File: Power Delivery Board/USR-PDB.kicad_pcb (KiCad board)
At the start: 2 copper layers, 110 x 150 mm, 35 parts, among them U1 XT90, U10 Anderson PP45 Vert. 2x1, U11 Anderson PP45 Vert. 2x1, U12 Anderson PP45 Vert. 2x1, U13 LM2575-5.0BT, U14 MCP3002-I/P, U2 Anderson PP45 Vert. 2x1, U3 Anderson PP45 Vert. 2x1, U4 Anderson PP45 Vert. 2x1, U5 Anderson PP45 Vert. 2x1, U6 Anderson PP45 Vert. 2x1, U7 LM2676T-12_NOPB

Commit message: updated PDB and analog board
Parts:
- added C8: 10uF, Capacitor_SMD:C_0805_2012Metric_Pad1.18x1.45mm_HandSolder, F.Cu at (125.5, 66.0)
- added C9: 10uF, Capacitor_SMD:C_0805_2012Metric_Pad1.18x1.45mm_HandSolder, F.Cu at (125.5, 59.5)
- added U17: AMS1117-3.3, USR:SOT_AMS1117-2.5_AMS, F.Cu at (118.5, 62.8)
- C1, C4: footprint Capacitor_THT:C_Disc_D5.0mm_W2.5mm_P2.50mm -> Capacitor_THT:C_Disc_D16.0mm_W5.0mm_P10.00mm
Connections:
- C6 pad 1: /5V_OUT -> 5V_OUT
- L2 pad 2: /5V_OUT -> 5V_OUT
- U1 pad N: (no net) -> GND
- U1 pad P: (no net) -> Vin
- U13 pad 4: /5V_OUT -> 5V_OUT
- U14 pad 8: /5V_OUT -> 3.3V_out
- U16 pad 2: /5V_OUT -> 5V_OUT
- U8 pad 14: /5V_OUT -> 5V_OUT
- U9 pad 14: /5V_OUT -> 5V_OUT
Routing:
- net 5V_OUT: track 0.00 -> 151.2 mm
- net /5V_OUT: track 140.8 -> 0.00 mm
- net 3.3V_out: track 0.00 -> 28.0 mm

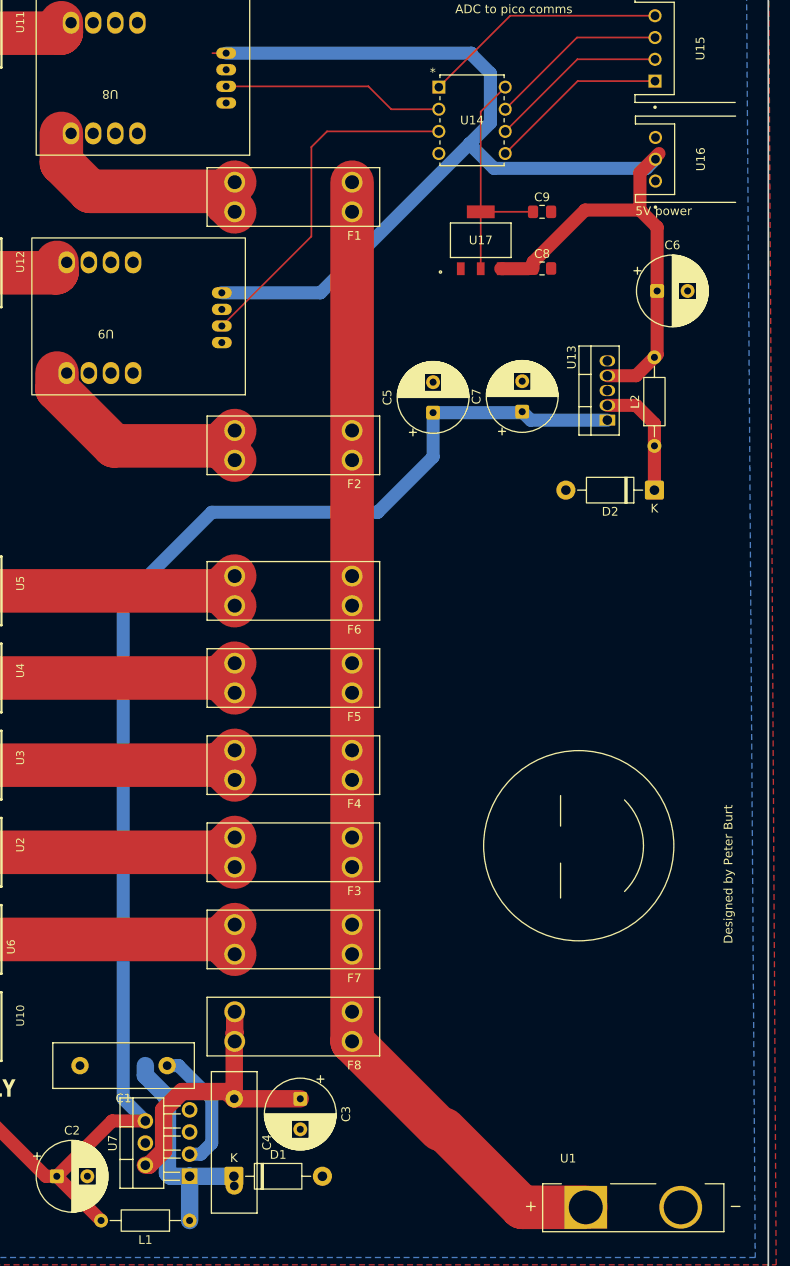
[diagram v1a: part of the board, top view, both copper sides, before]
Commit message: Added 3.3V regulator to PDB board
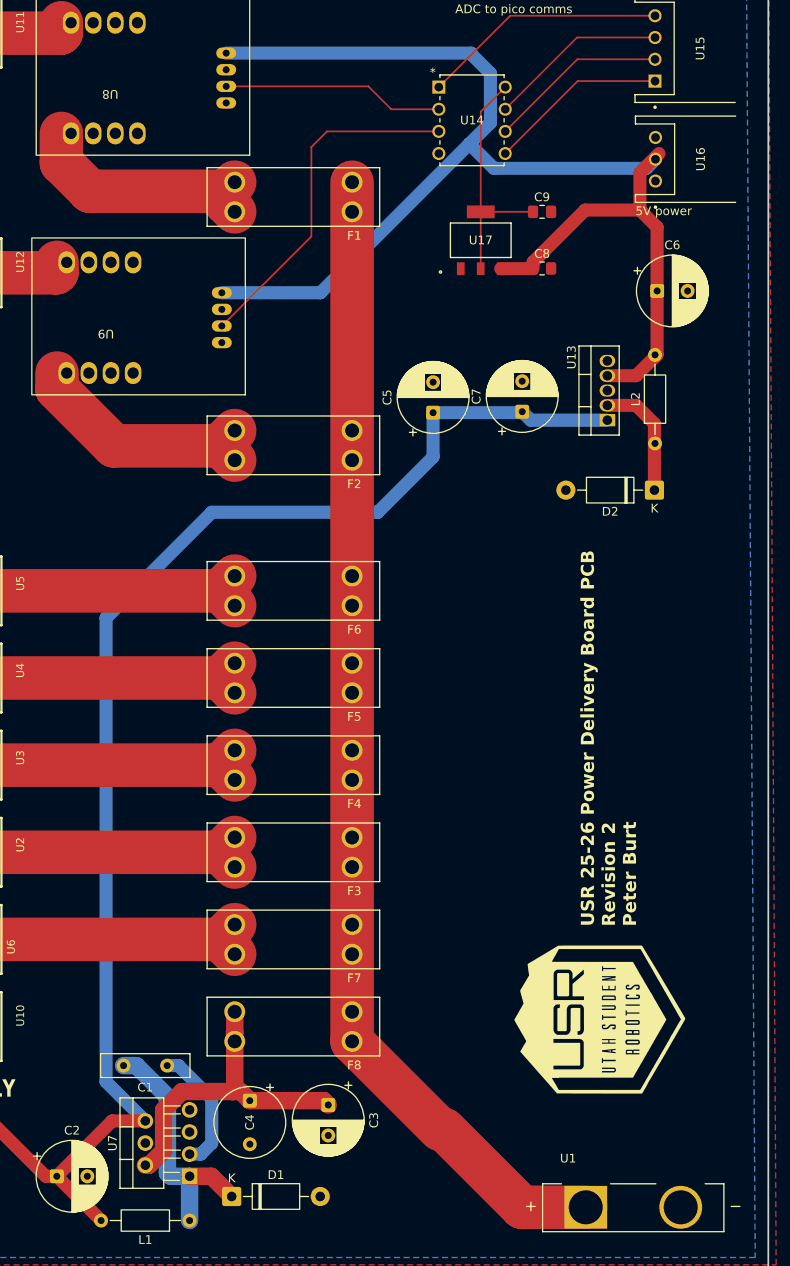
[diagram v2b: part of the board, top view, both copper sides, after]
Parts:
- C1: footprint Capacitor_THT:C_Disc_D16.0mm_W5.0mm_P10.00mm -> Capacitor_THT:C_Disc_D10.0mm_W2.5mm_P5.00mm
- C4: footprint Capacitor_THT:C_Disc_D16.0mm_W5.0mm_P10.00mm -> Capacitor_THT:CP_Radial_Tantal_D8.0mm_P5.00mm
- moved C3 3.29 mm to (101.0, 162.0)
- moved D1 2.33 mm to (89.9, 172.5)
- moved C4 1.80 mm to (92.0, 161.5)
- moved L2 0.29 mm to (138.5, 86.1)
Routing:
- net Net-(D1-K): track 26.2 -> 28.8 mm
- net Net-(U7-VIN): track 35.4 -> 37.2 mm
- net /12V_OUT: track 172.1 -> 173.7 mm
- net 5V_OUT: track 151.2 -> 149.6 mm
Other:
- board text added: "USR 25-26 Power Delivery Board PCB Revision 2 Peter Burt"
- board text removed: "Designed by Peter Burt"

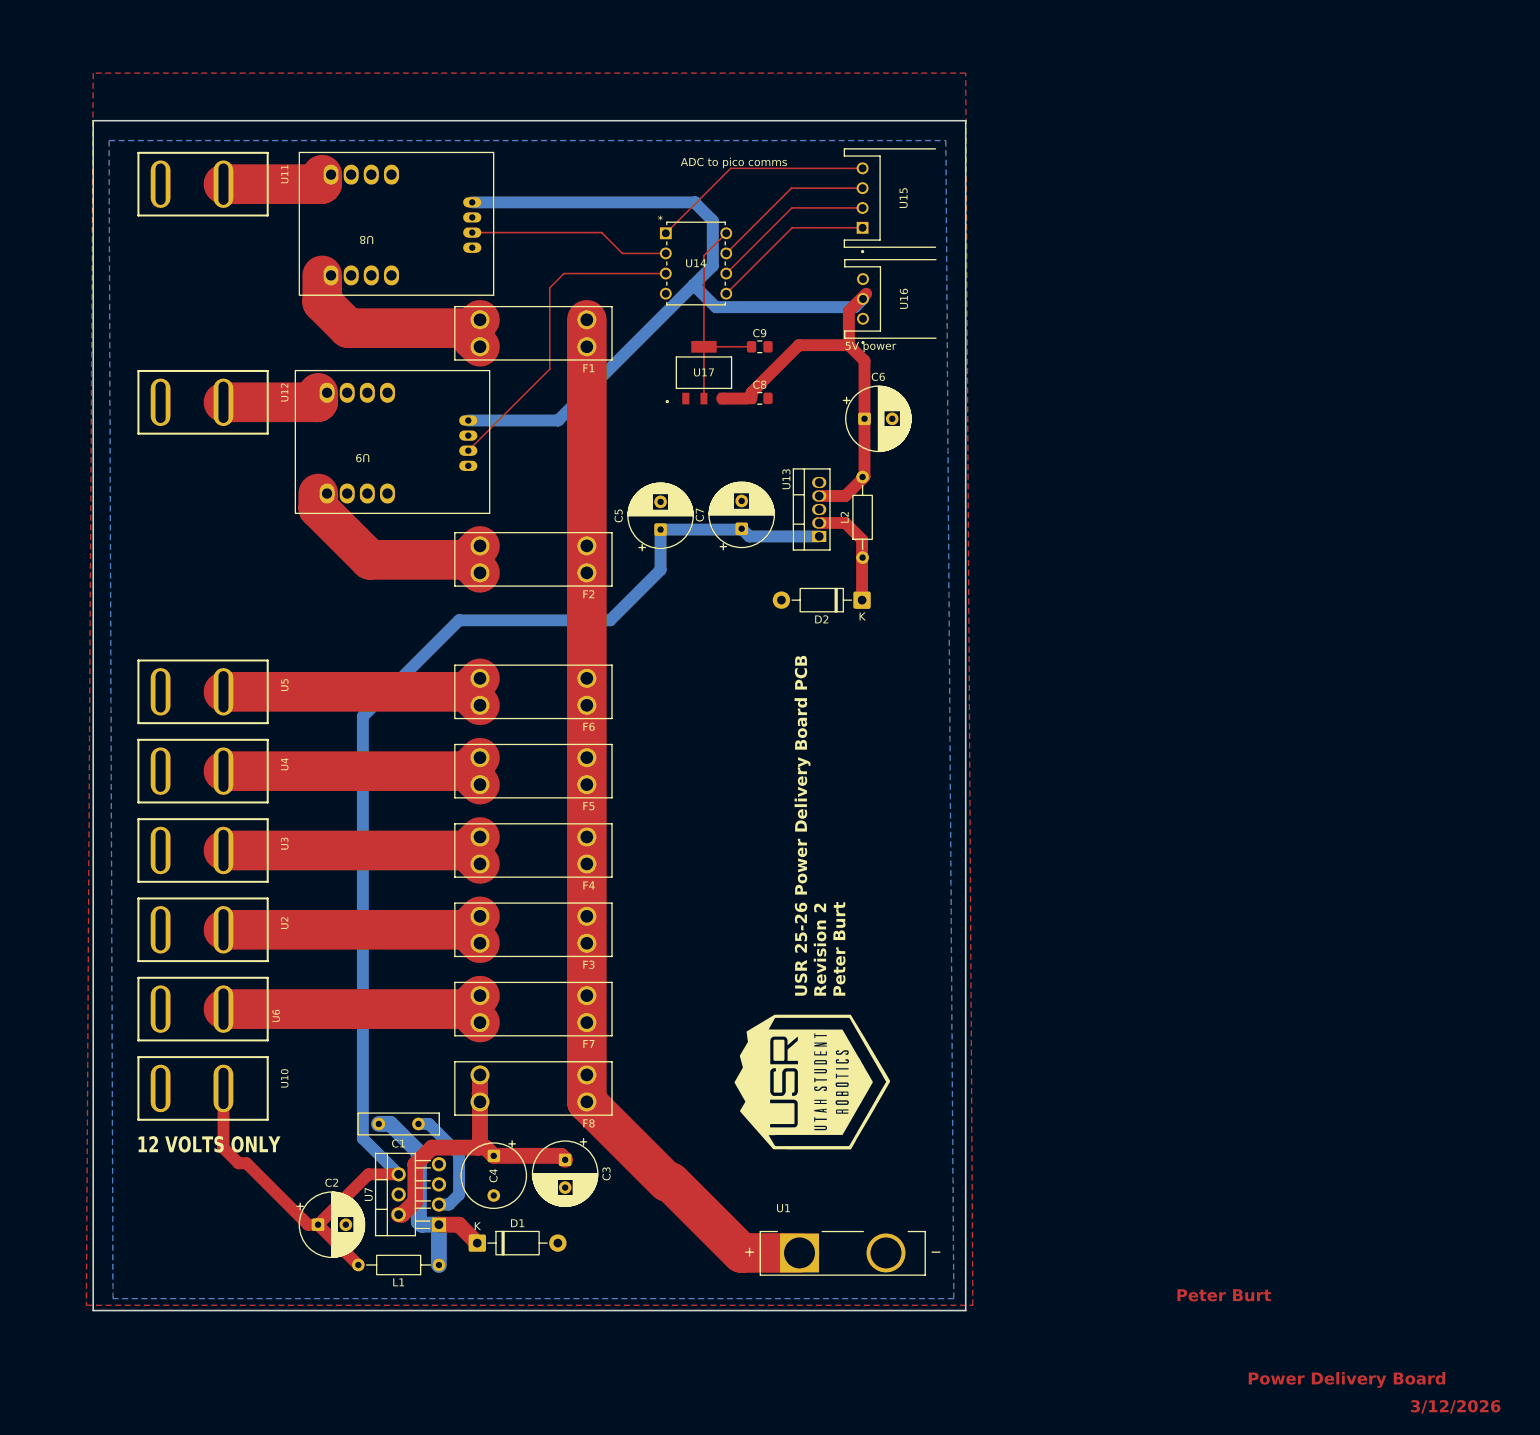
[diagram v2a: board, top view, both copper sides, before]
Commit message: Updated MCU card and PDB
MCU card schematic is laid out (tentative but likely final)
PDB has had minor trace width updates
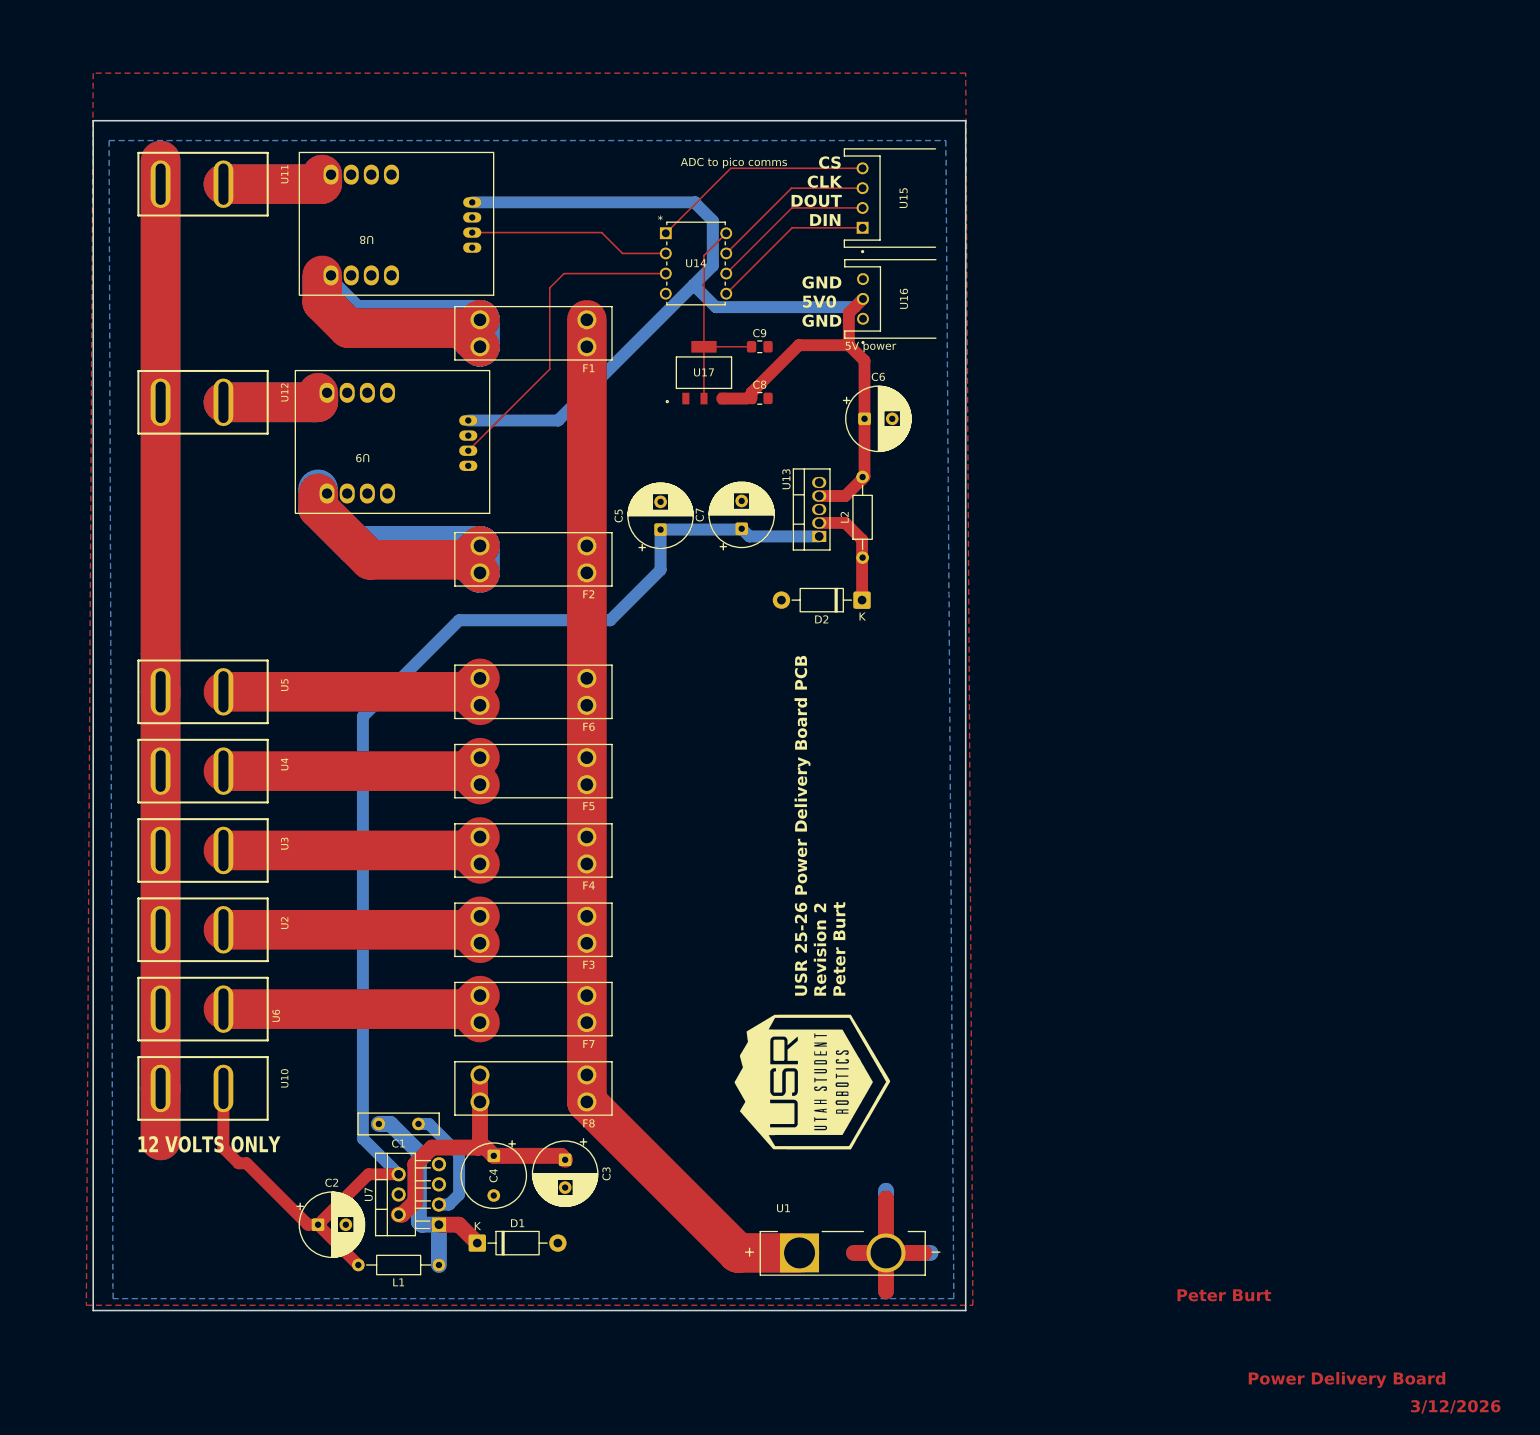
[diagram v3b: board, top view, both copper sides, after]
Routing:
- net GND: track 0.00 -> 290.0 mm
- net HE_sensor2: track 28.1 -> 66.6 mm
- net HE_sensor1: track 27.8 -> 59.5 mm
- net Net-(U12-VCC): track 14.8 -> 28.6 mm
- net Net-(U11-VCC): track 15.3 -> 28.9 mm
- net 5V_OUT: track 149.6 -> 148.8 mm
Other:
- board text added: "CS CLK DOUT DIN"
- board text added: "GND 5V0 GND"

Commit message: replaced LM2575 volt. regulator with 2x LM7805 in parallel
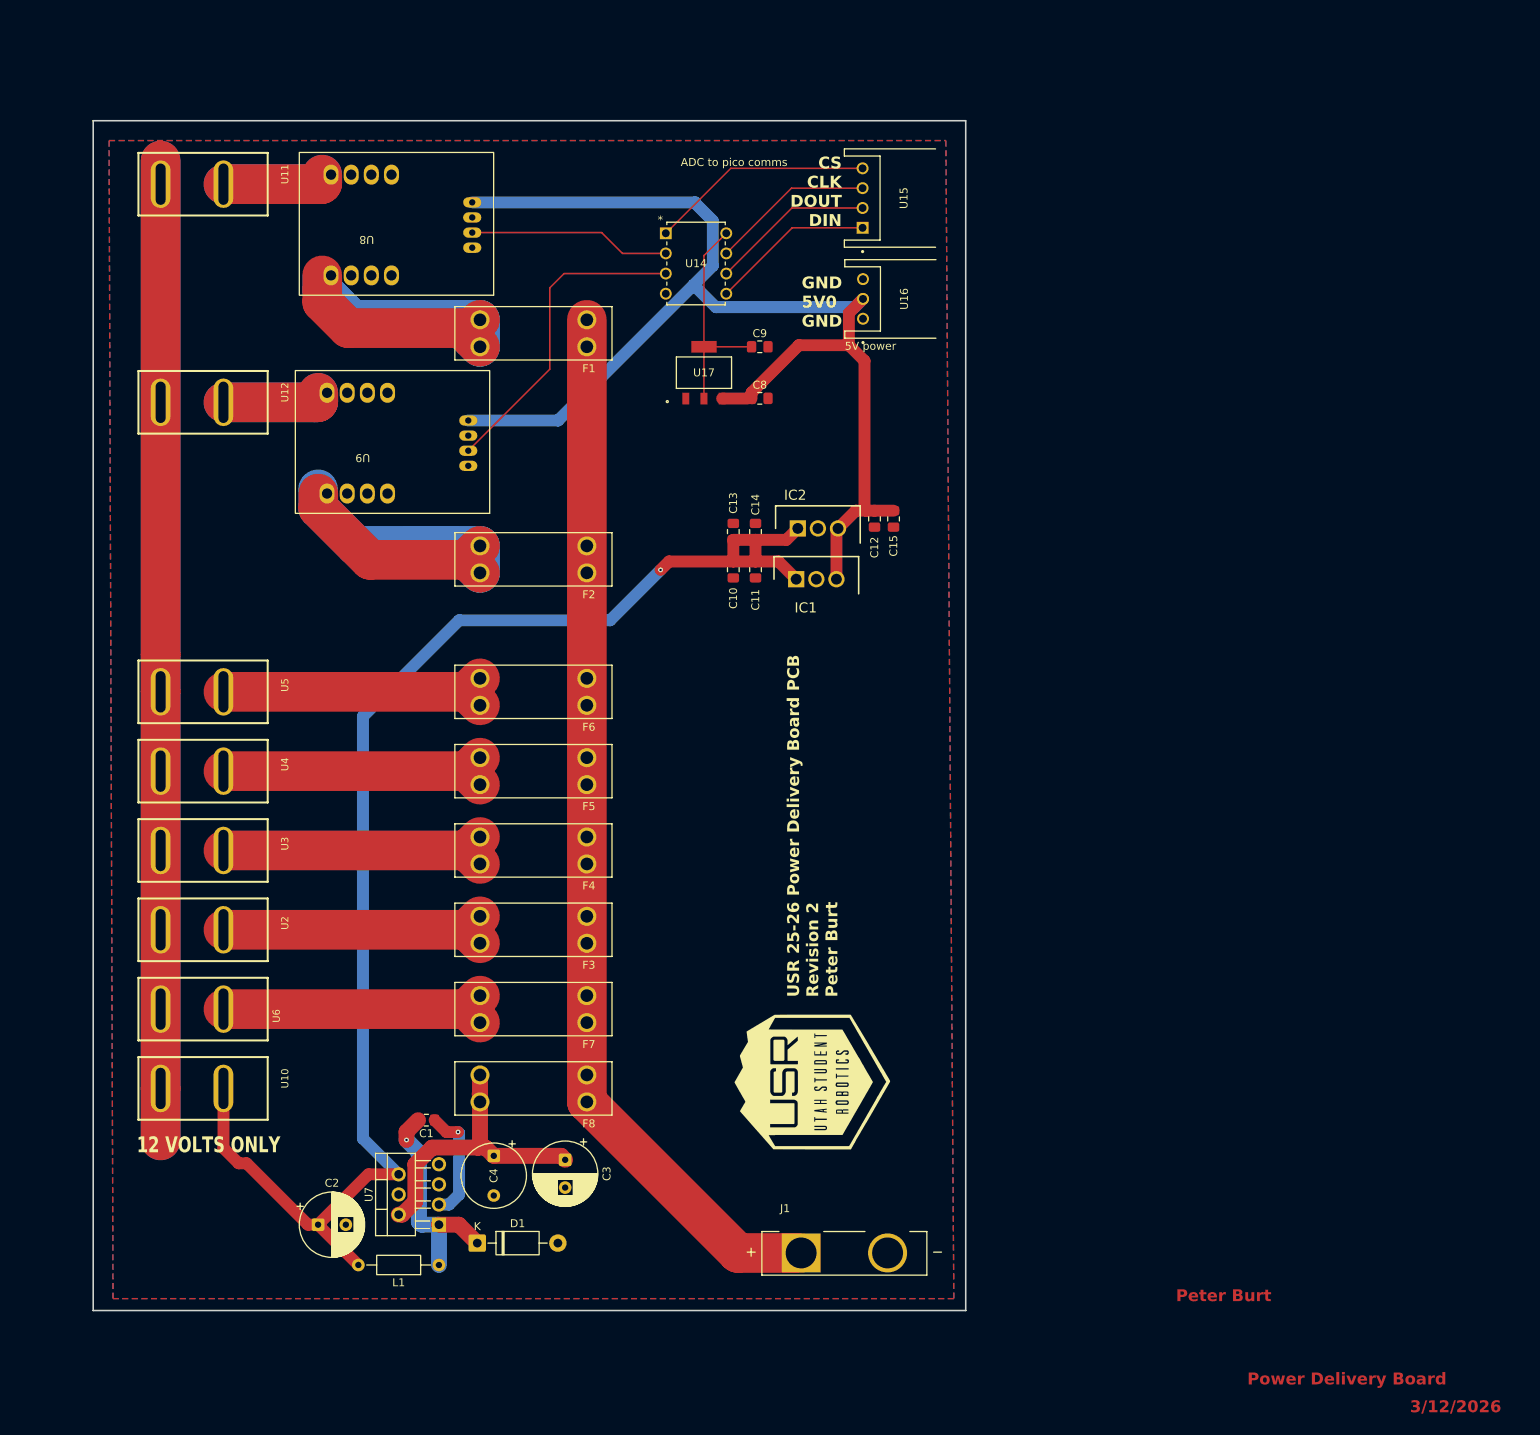
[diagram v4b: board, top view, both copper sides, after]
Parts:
- removed C5: 47uF, Capacitor_THT:CP_Radial_D8.0mm_P3.50mm
- removed C6: 470uF, Capacitor_THT:CP_Radial_D8.0mm_P3.50mm
- removed C7: 22uF, Capacitor_THT:CP_Radial_D8.0mm_P3.50mm
- removed D2: SS24FL (550mV 2A), Diode_THT:D_DO-41_SOD81_P10.16mm_Horizontal
- removed L2: 220uH, Inductor_THT:L_Axial_L5.3mm_D2.2mm_P10.16mm_Horizontal_Vishay_IM-1
- removed U1: XT90, USR:AMASS_XT90PW-M_VERTICAL
- removed U13: LM2575-5.0BT, Package_TO_SOT_THT:TO-220-5_Vertical
- added C10: 100nF, Capacitor_SMD:C_0805_2012Metric_Pad1.18x1.45mm_HandSolder, F.Cu at (122.2, 87.6)
- added C11: 100nF, Capacitor_SMD:C_0805_2012Metric_Pad1.18x1.45mm_HandSolder, F.Cu at (125.0, 87.6)
- added C12: 100nF, Capacitor_SMD:C_0805_2012Metric_Pad1.18x1.45mm_HandSolder, F.Cu at (140.0, 81.2)
- added C13: 100nF, Capacitor_SMD:C_0805_2012Metric_Pad1.18x1.45mm_HandSolder, F.Cu at (122.2, 82.8)
- added C14: 100nF, Capacitor_SMD:C_0805_2012Metric_Pad1.18x1.45mm_HandSolder, F.Cu at (125.0, 82.8)
- added C15: 100nF, Capacitor_SMD:C_0805_2012Metric_Pad1.18x1.45mm_HandSolder, F.Cu at (142.4, 81.2)
- added IC1: LM7805ECT, USR:LM7805ECT, F.Cu at (130.1, 88.8)
- added IC2: LM7805ECT, USR:LM7805ECT, F.Cu at (130.3, 82.4)
- added J1: XT90PW-M, USR:AMASS_XT90PW-M_VERTICAL, F.Cu at (136.2, 174.0)
- C1: footprint Capacitor_THT:C_Disc_D10.0mm_W2.5mm_P5.00mm -> Capacitor_SMD:C_0805_2012Metric_Pad1.18x1.45mm_HandSolder
- moved C1 1.10 mm to (83.5, 157.0)
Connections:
- net /12V_OUT renamed 12V_OUT
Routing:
- net GND: track 290.0 -> 247.0 mm
- net Net-(D2-K): track 13.9 -> 0.00 mm
- net 5V_OUT: track 148.8 -> 160.8 mm
- net 12V_OUT: track 173.7 -> 180.8 mm, vias 0 -> 1
- net Net-(D1-K): track 28.8 -> 27.6 mm, vias 0 -> 1
- net Net-(U7-BOOST): track 14.8 -> 14.6 mm, vias 0 -> 1
